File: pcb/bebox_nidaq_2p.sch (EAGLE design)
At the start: 6 parts, among them J1 1-1634612-0, J2 1-1634612-0, J6 SJ-435107RS, U1 MCP23008-E/P, U2 MCP23008-E/P, X1 71430-0101

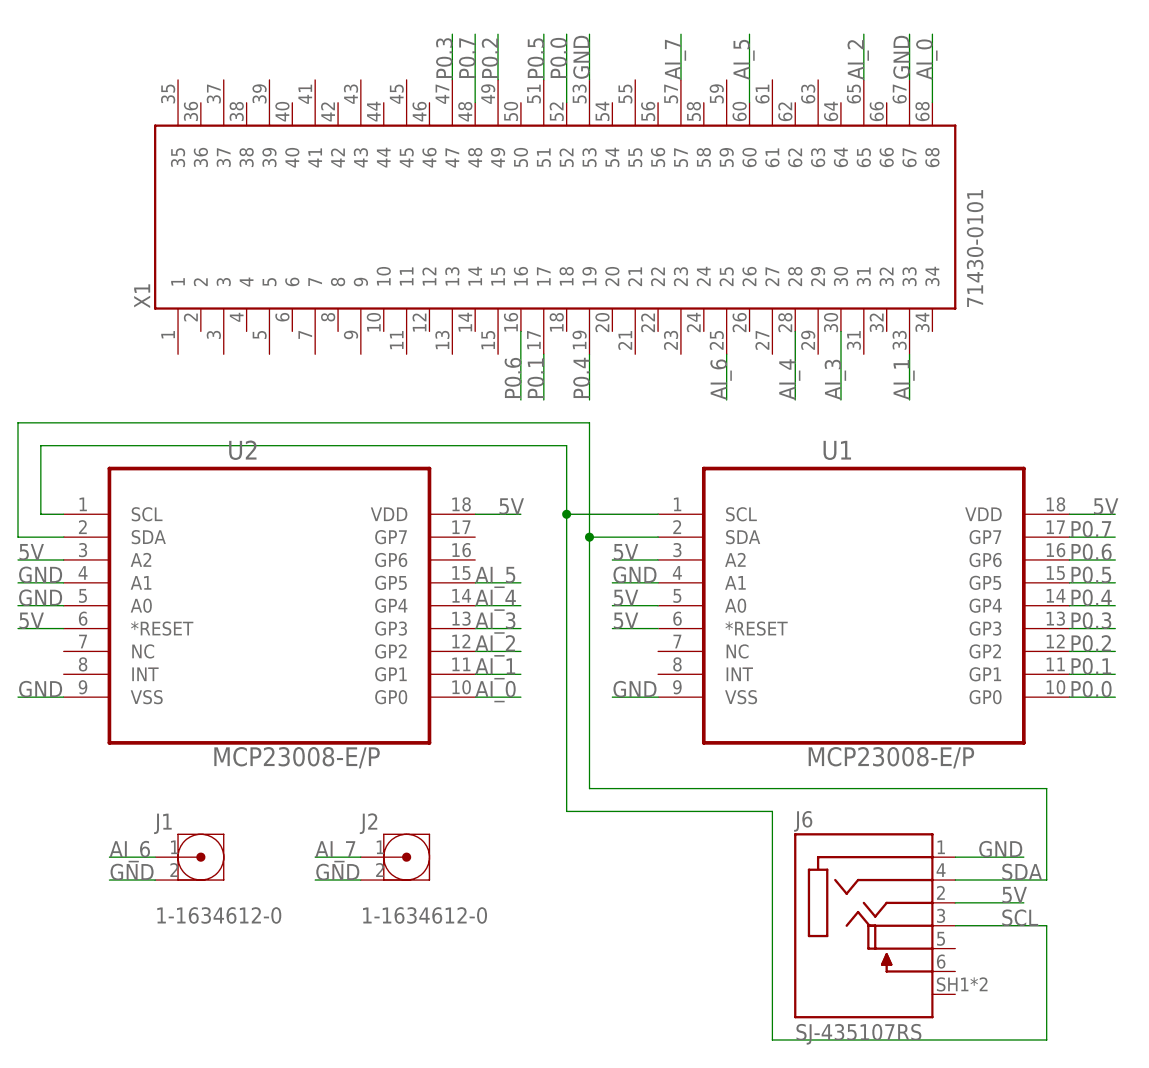
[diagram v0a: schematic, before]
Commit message: Previously did not have sufficient analog inputs for two photometry inputs and one digital input. Now have 4 BNC inputs.
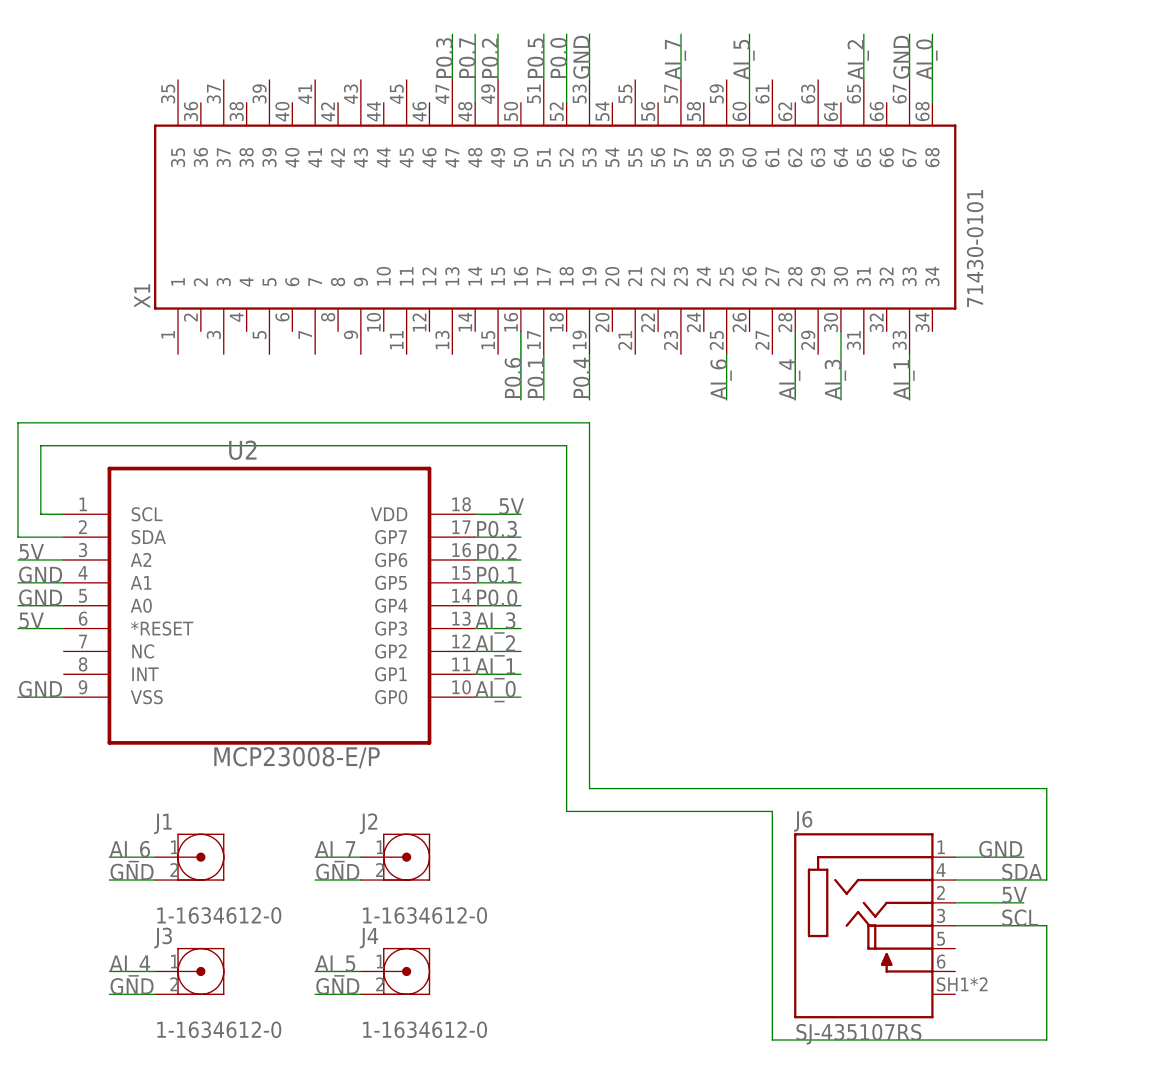
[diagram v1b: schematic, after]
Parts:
- removed U1: MCP23008-E/P, MCP23008-E_P:MCP23008-E/P
- added J3, J4: 1-1634612-0, 1-1634612-0:1-1634612-0
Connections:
- net 5V: no longer U1.*RESET, U1.A0, U1.A2, U1.VDD
- net AI_4: now also J3.1; no longer U2.GP4
- net AI_5: now also J4.1; no longer U2.GP5
- net GND: now also J3.2, J4.2; no longer U1.A1, U1.VSS
- net P0.0: now also U2.GP4; no longer U1.GP0
- net P0.1: now also U2.GP5; no longer U1.GP1
- net P0.2: now also U2.GP6; no longer U1.GP2
- net P0.3: now also U2.GP7; no longer U1.GP3
- net P0.4: no longer U1.GP4
- net P0.5: no longer U1.GP5
- net P0.6: no longer U1.GP6
- net P0.7: no longer U1.GP7
- net SCL: no longer U1.SCL
- net SDA: no longer U1.SDA
